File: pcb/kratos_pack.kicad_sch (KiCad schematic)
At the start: 96 parts, among them J1 USB_C_Receptacle_USB2.0, J2 PROG_CONN, J3 DBG_UART, J4 BAT_MID+NTC, J5 BAT_7.4V, J6 BAT_0V, J7 OUT+, J8 OUT-, Q1 AON7403, Q2 AON7414, Q3 AON7414, SW1 WAKEUP, SW2 BOOT, SW3 RST_BTN, U1 USBLC6-2SC6, U10 24LC32, U2 CP2102N-Axx-xQFN20, U3 STM32G071Gx, U4 KTD2026BEWE, U5 BQ25887, U6 BD48xxFVE, U7 INA199, U8 LTC4231, U9 LDK715M33R

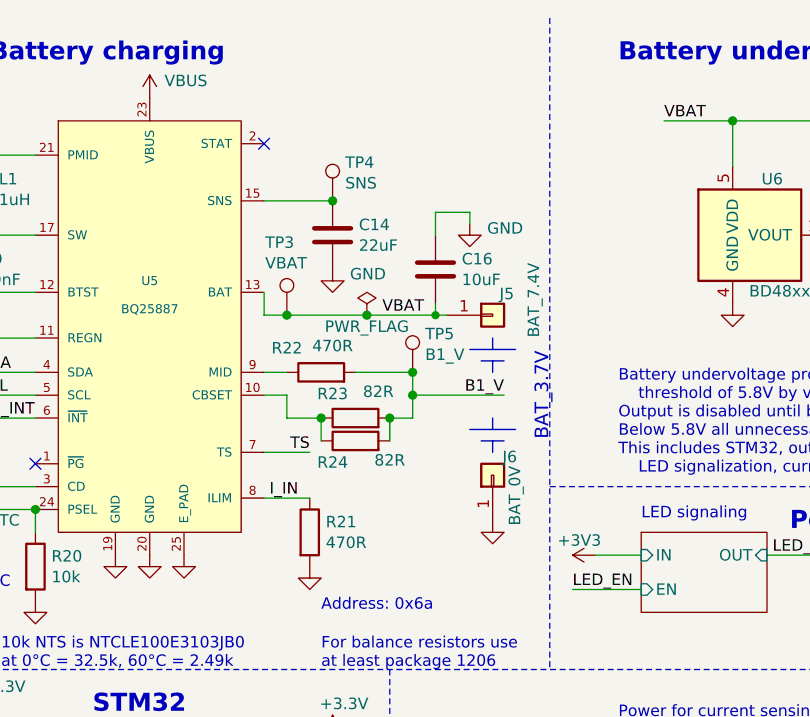
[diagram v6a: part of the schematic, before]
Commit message: Schema & PCB: exchange SNS capacitor of charger IC for 47uF/16V in 1206
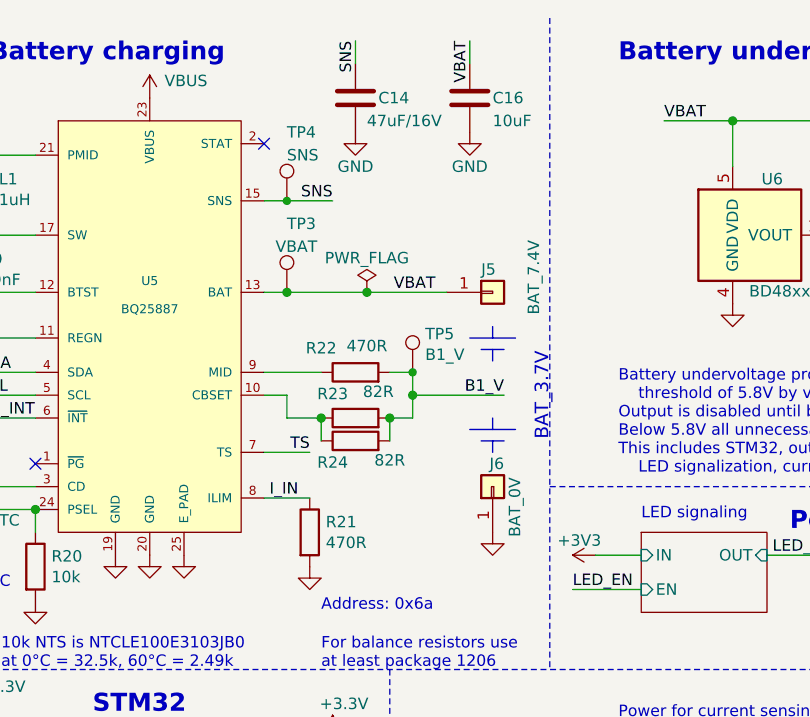
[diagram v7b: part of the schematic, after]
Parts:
- C14: value 22uF -> 47uF/16V; footprint TCY_passives:C_0805_2012Metric -> TCY_passives:C_1206_3216Metric
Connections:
- net GND: now also C16.2; no longer C16.1
- net VBAT: now also C16.1; no longer C16.2
- net SNS: now reaches C14.1, TP4.1, U5.15 (SNS), U5.16 (SNS)
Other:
- moved on the sheet: C14, C16, J5, J6, R22, TP3, TP4

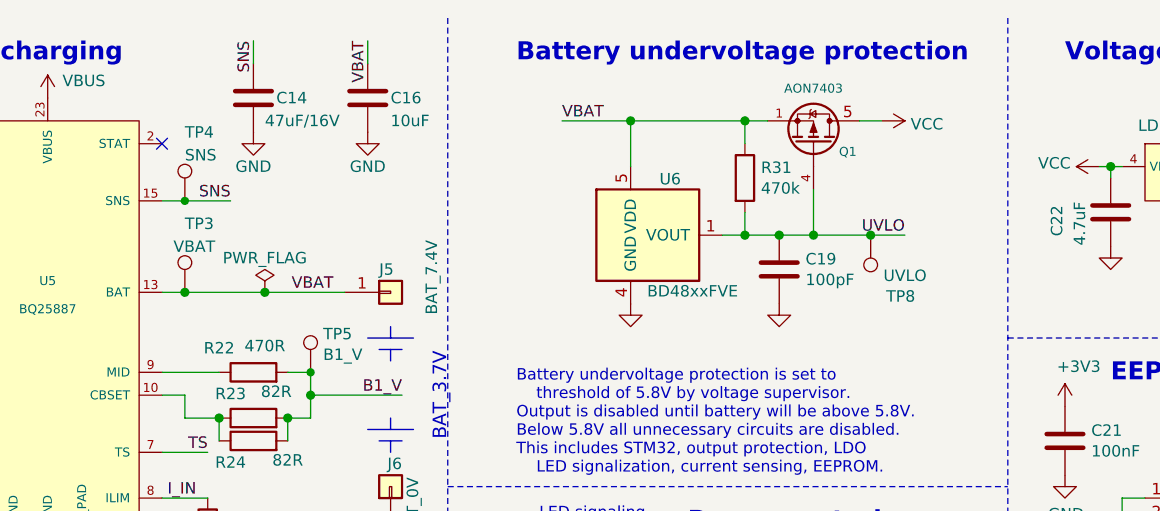
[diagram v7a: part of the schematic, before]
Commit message: Schema & PCB: fix under-voltage supervisor by inverting output signal
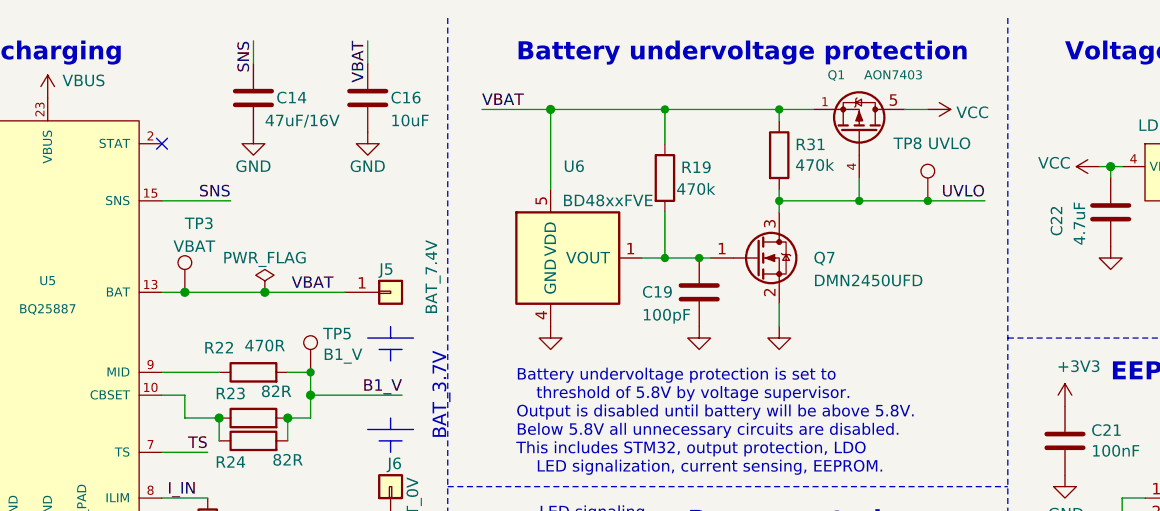
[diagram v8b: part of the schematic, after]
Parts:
- removed TP4: SNS, TCY_connectors:TestPoint_Pad_D0.5mm, symbol Connector:TestPoint
- added Q7: DMN2450UFD, TCY_IC:DFN-3_1.2x1.2mm, symbol TCY_transistors:DMN2450UFD
- added R19: 470k, TCY_passives:R_0603_1608Metric, symbol Device:R
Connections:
- net GND: now also Q7.2 (S)
- net UVLO: now also Q7.3 (D); no longer C19.1, U6.1 (VOUT)
- net VBAT: now also R19.1
- new net: C19.1, Q7.1 (G), R19.2, U6.1 (VOUT)
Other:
- moved on the sheet: C19, Q1, R31, TP8, U6
